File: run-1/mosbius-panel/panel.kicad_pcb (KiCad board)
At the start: 4 copper layers, 84 x 82 mm, 60 parts, among them J101 Conn_02x35_Counter_Clockwise_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, J102 Conn_02x35_Counter_Clockwise_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, J103 Conn_02x35_Counter_Clockwise_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, J104 Conn_02x35_Counter_Clockwise_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, J105 Conn_02x35_Counter_Clockwise_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, J106 Conn_02x35_Counter_Clockwise_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, J107 Conn_02x35_Counter_Clockwise_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, J108 Conn_02x35_Counter_Clockwise_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, J109 Conn_02x35_Counter_Clockwise_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, J110 Conn_02x35_Counter_Clockwise_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

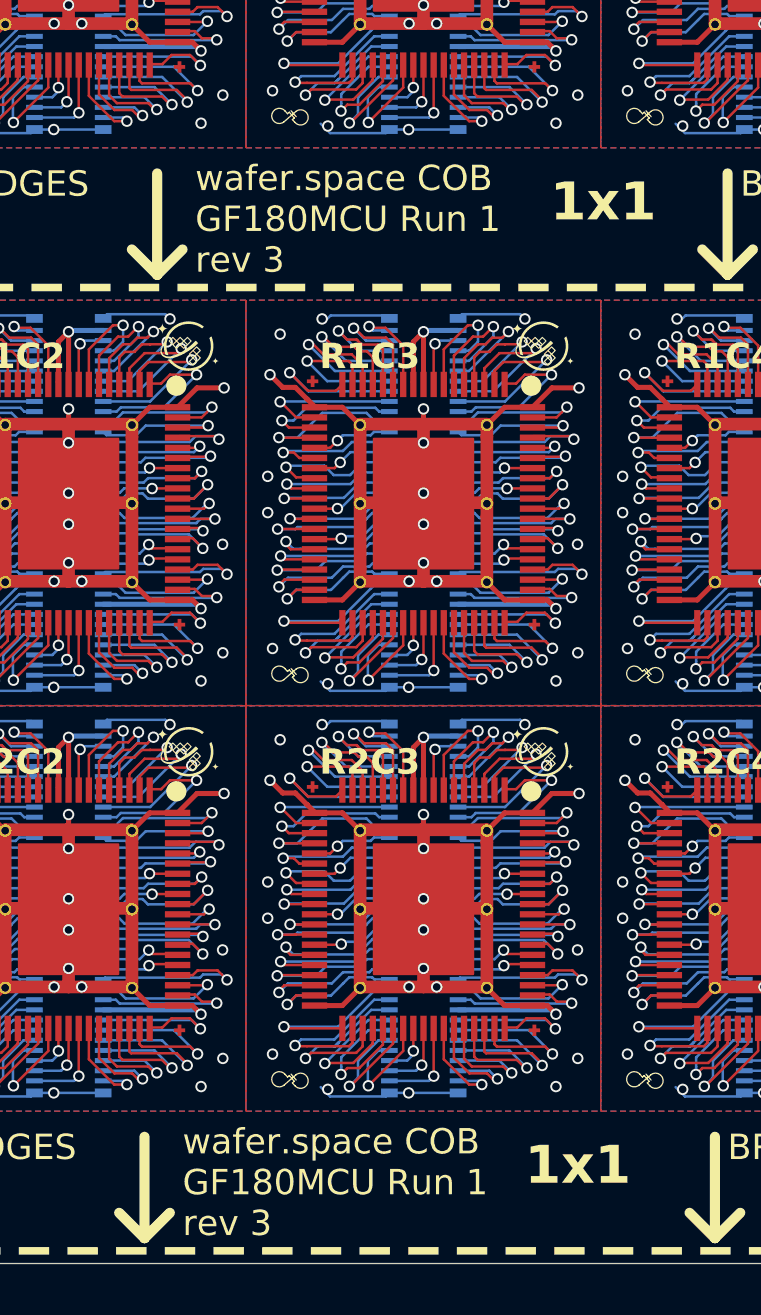
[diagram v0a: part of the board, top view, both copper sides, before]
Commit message: fix silkscreen for name
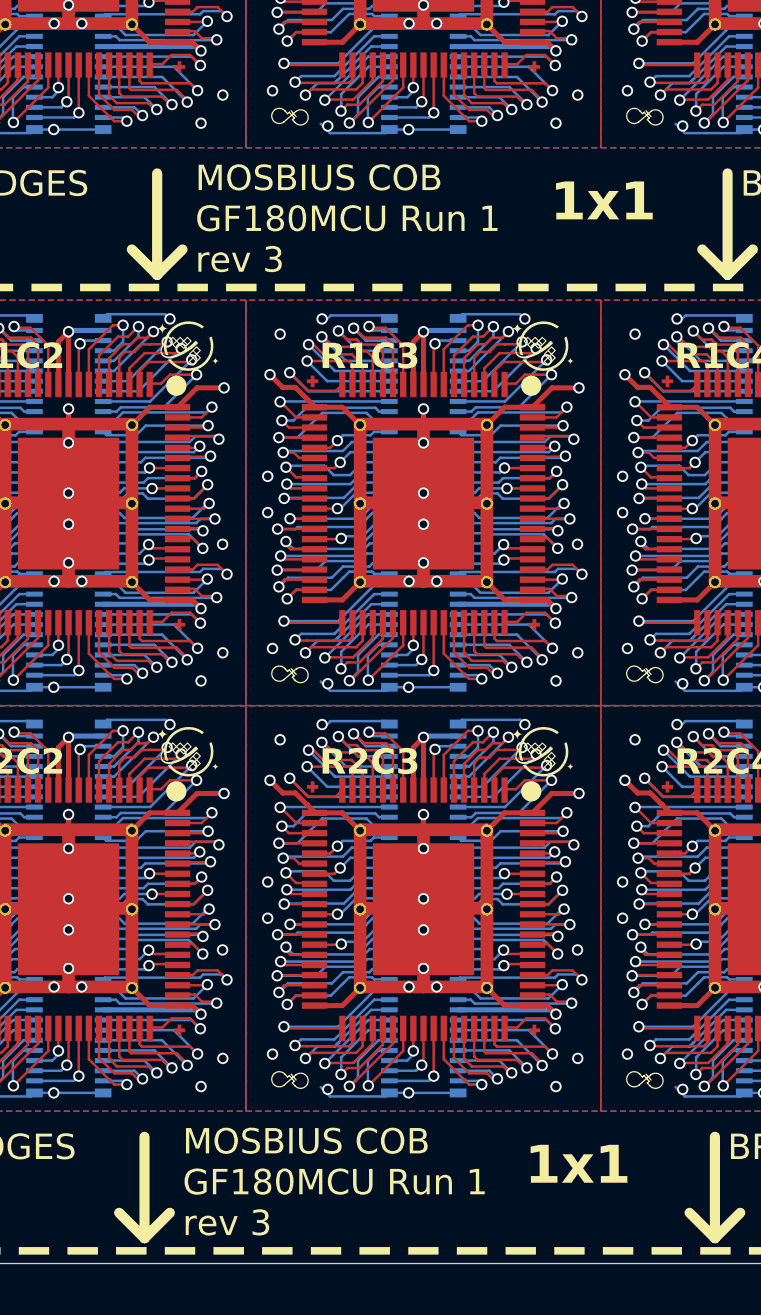
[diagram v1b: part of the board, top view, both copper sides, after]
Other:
- board text added: "MOSBIUS COB GF180MCU Run 1 rev 3"
- board text removed: "wafer.space COB GF180MCU Run 1 rev 3"
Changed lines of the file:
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@@
 		)
 	)
-	(gr_text "wafer.space COB\nGF180MCU Run 1\nrev 3"
+	(gr_text "MOSBIUS COB\nGF180MCU Run 1\nrev 3"
 		(at 89.32 125.39 0)
 		(layer "F.SilkS")
@@
 		)
 	)
-	(gr_text "wafer.space COB\nGF180MCU Run 1\nrev 3"
+	(gr_text "MOSBIUS COB\nGF180MCU Run 1\nrev 3"
 		(at 89.82 87.39 0)
 		(layer "F.SilkS")
